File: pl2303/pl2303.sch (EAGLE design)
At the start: 3 parts, among them J1 ESP-STACK-HEADER, SW1 SW_TACT_2P-3X6

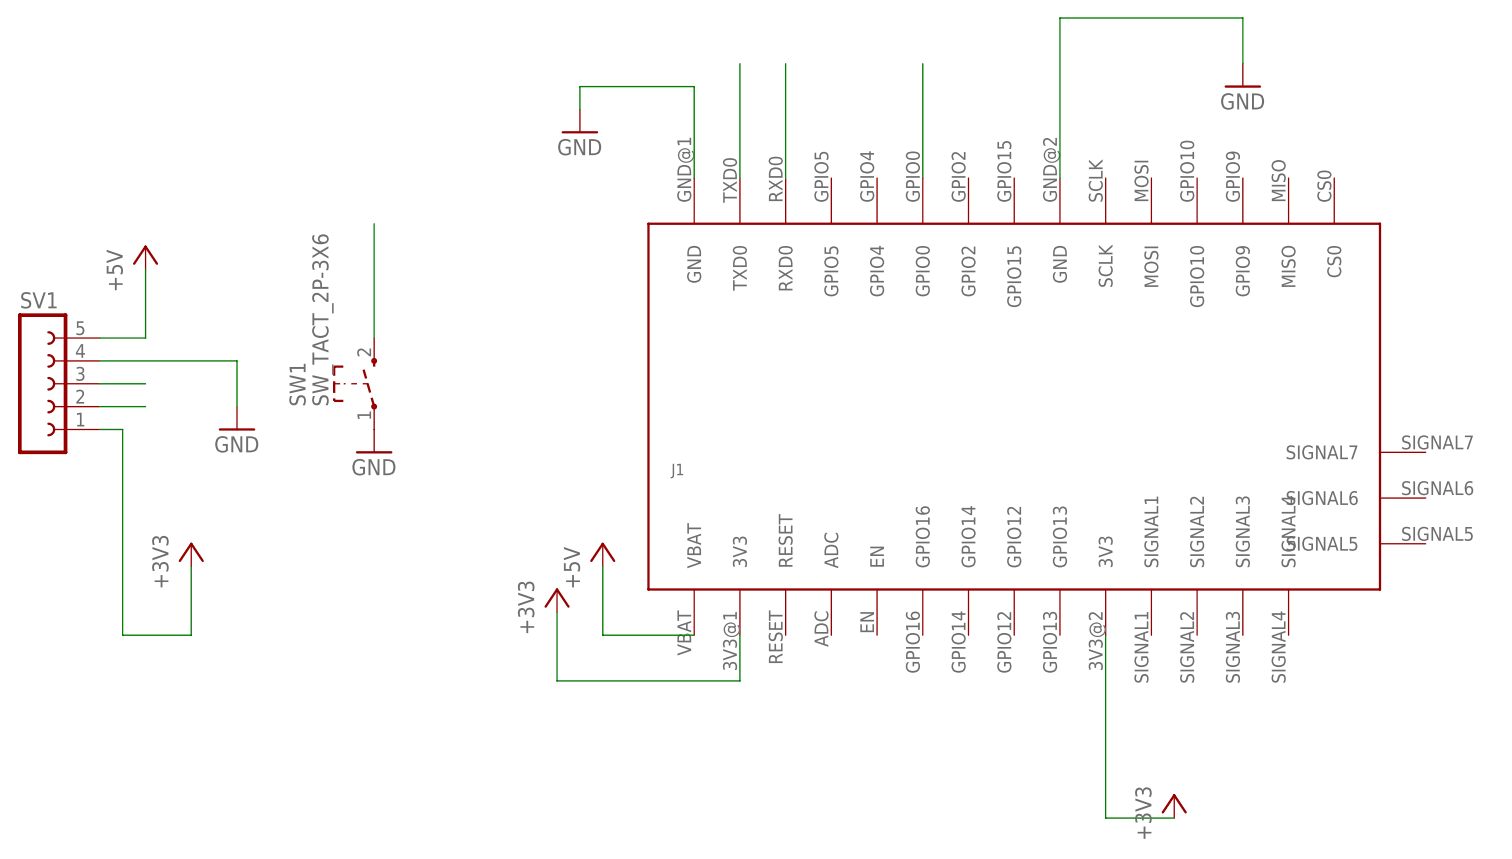
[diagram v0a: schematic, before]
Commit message: FTDI board update - new board size and mounting holes
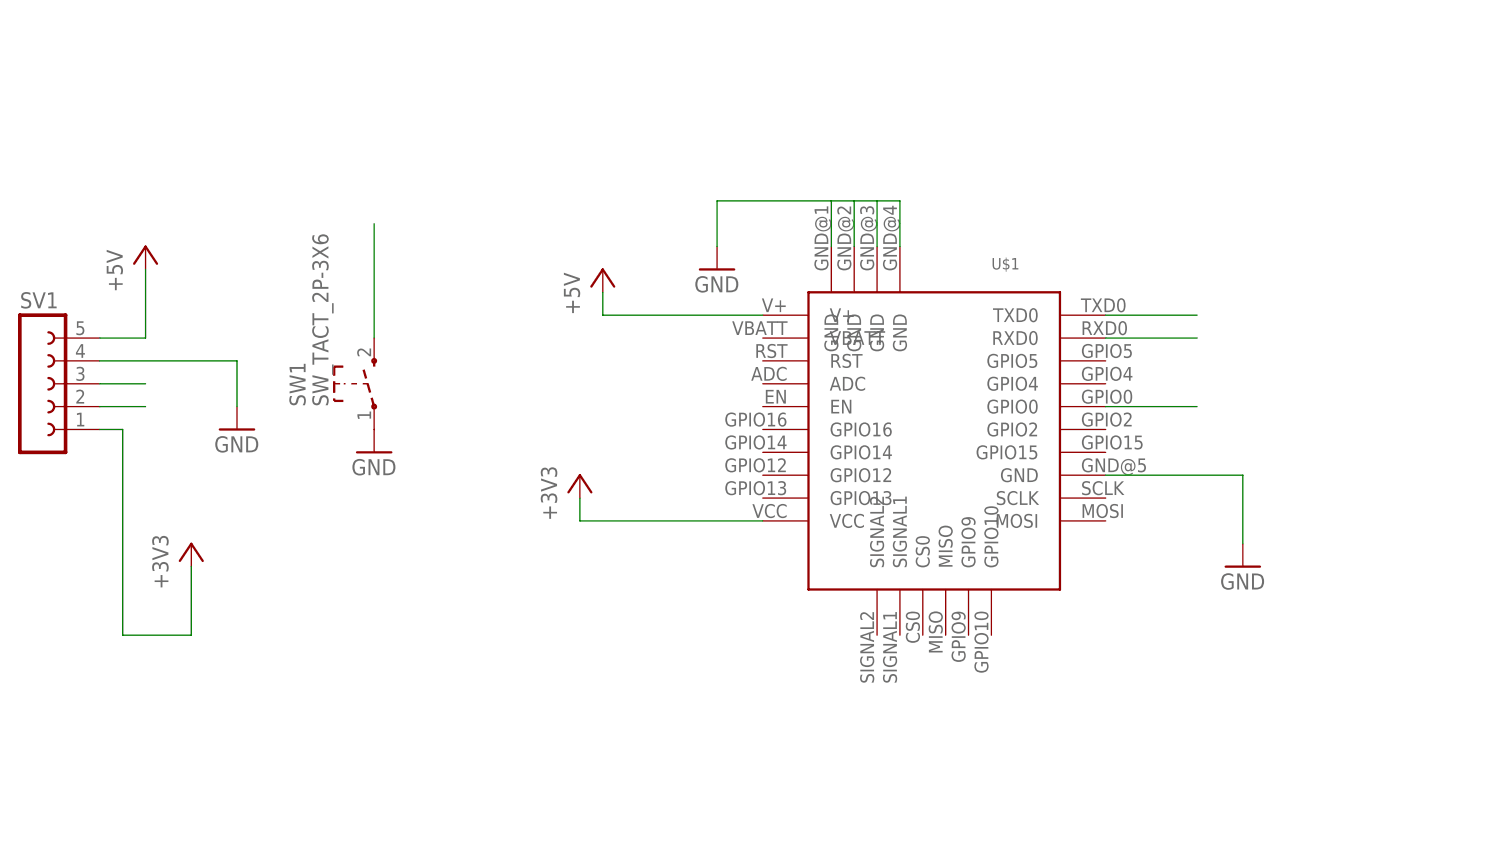
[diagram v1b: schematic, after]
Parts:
- removed J1: ESP-STACK-HEADER, ESPstack:ESP-STACK-HEADER
- added U$1: ESP-BOARD, ESPstack:ESP-BOARD
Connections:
- net +3V3: now also U$1.VCC; no longer J1.3V3@1, J1.3V3@2
- net +5V: now also U$1.V+; no longer J1.VBAT
- net GND: now also U$1.GND@1, U$1.GND@2, U$1.GND@3, U$1.GND@4, U$1.GND@5; no longer J1.GND@1, J1.GND@2
- net GPIO0: now also U$1.GPIO0; no longer J1.GPIO0
- net RXD0: now also U$1.RXD0; no longer J1.RXD0
- net TXD0: now also U$1.TXD0; no longer J1.TXD0
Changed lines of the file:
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@@
 <part name="P+1" library="supply1" deviceset="+5V" device=""/>
 <part name="+3V2" library="supply1" deviceset="+3V3" device=""/>
-<part name="J1" library="ESPstack" deviceset="ESP-STACK-HEADER" device=""/>
 <part name="+3V1" library="supply1" deviceset="+3V3" device=""/>
-<part name="+3V3" library="supply1" deviceset="+3V3" device=""/>
 <part name="P+2" library="supply1" deviceset="+5V" device=""/>
 <part name="GND1" library="supply1" deviceset="GND" device=""/>
@@
 <part name="SW1" library="dp_devices" deviceset="SW_TACT_2P" device="-3X6"/>
 <part name="GND4" library="supply1" deviceset="GND" device=""/>
+<part name="U$1" library="ESPstack" deviceset="ESP-BOARD" device=""/>
 </parts>
 <sheets>
@@
 <instance part="P+1" gate="1" x="7.62" y="71.12"/>
 <instance part="+3V2" gate="G$1" x="12.7" y="38.1"/>
-<instance part="J1" gate="G$1" x="83.82" y="53.34"/>
-<instance part="+3V1" gate="G$1" x="53.34" y="33.02"/>
-<instance part="+3V3" gate="G$1" x="121.92" y="10.16"/>
-<instance part="P+2" gate="1" x="58.42" y="38.1"/>
-<instance part="GND1" gate="1" x="129.54" y="88.9"/>
-<instance part="GND3" gate="1" x="55.88" y="83.82"/>
+<instance part="+3V1" gate="G$1" x="55.88" y="45.72"/>
+<instance part="P+2" gate="1" x="58.42" y="68.58"/>
+<instance part="GND1" gate="1" x="129.54" y="35.56"/>
+<instance part="GND3" gate="1" x="71.12" y="68.58"/>
 <instance part="SW1" gate="SW" x="33.02" y="55.88" rot="R90"/>
 <instance part="GND4" gate="1" x="33.02" y="48.26"/>
+<instance part="U$1" gate="G$1" x="93.98" y="50.8"/>
 </instances>
 <busses>
@@
 <net name="GND" class="0">
 <segment>
-<pinref part="J1" gate="G$1" pin="GND@2"/>
-<wire x1="109.22" y1="78.74" x2="109.22" y2="96.52" width="0.1524" layer="91"/>
-<wire x1="109.22" y1="96.52" x2="129.54" y2="96.52" width="0.1524" layer="91"/>
+<wire x1="129.54" y1="45.72" x2="129.54" y2="38.1" width="0.1524" layer="91"/>
 <pinref part="GND1" gate="1" pin="GND"/>
-<wire x1="129.54" y1="96.52" x2="129.54" y2="91.44" width="0.1524" layer="91"/>
+<pinref part="U$1" gate="G$1" pin="GND@5"/>
+<wire x1="129.54" y1="45.72" x2="114.3" y2="45.72" width="0.1524" layer="91"/>
 </segment>
 <segment>
-<pinref part="J1" gate="G$1" pin="GND@1"/>
-<wire x1="68.58" y1="78.74" x2="68.58" y2="88.9" width="0.1524" layer="91"/>
-<wire x1="68.58" y1="88.9" x2="55.88" y2="88.9" width="0.1524" layer="91"/>
-<wire x1="55.88" y1="88.9" x2="55.88" y2="86.36" width="0.1524" layer="91"/>
+<wire x1="91.44" y1="76.2" x2="88.9" y2="76.2" width="0.1524" layer="91"/>
+<wire x1="88.9" y1="76.2" x2="86.36" y2="76.2" width="0.1524" layer="91"/>
+<wire x1="86.36" y1="76.2" x2="83.82" y2="76.2" width="0.1524" layer="91"/>
+<wire x1="83.82" y1="76.2" x2="71.12" y2="76.2" width="0.1524" layer="91"/>
+<wire x1="71.12" y1="76.2" x2="71.12" y2="71.12" width="0.1524" layer="91"/>
 <pinref part="GND3" gate="1" pin="GND"/>
+<pinref part="U$1" gate="G$1" pin="GND@1"/>
+<wire x1="83.82" y1="71.12" x2="83.82" y2="76.2" width="0.1524" layer="91"/>
+<pinref part="U$1" gate="G$1" pin="GND@2"/>
+<wire x1="86.36" y1="71.12" x2="86.36" y2="76.2" width="0.1524" layer="91"/>
+<pinref part="U$1" gate="G$1" pin="GND@3"/>
+<wire x1="88.9" y1="71.12" x2="88.9" y2="76.2" width="0.1524" layer="91"/>
+<pinref part="U$1" gate="G$1" pin="GND@4"/>
+<wire x1="91.44" y1="76.2" x2="91.44" y2="71.12" width="0.1524" layer="91"/>
 </segment>
 <segment>
@@
 <net name="+5V" class="0">
 <segment>
-<pinref part="J1" gate="G$1" pin="VBAT"/>
-<wire x1="68.58" y1="27.94" x2="58.42" y2="27.94" width="0.1524" layer="91"/>
-<wire x1="58.42" y1="27.94" x2="58.42" y2="35.56" width="0.1524" layer="91"/>
+<wire x1="58.42" y1="63.5" x2="58.42" y2="66.04" width="0.1524" layer="91"/>
 <pinref part="P+2" gate="1" pin="+5V"/>
+<pinref part="U$1" gate="G$1" pin="V+"/>
+<wire x1="58.42" y1="63.5" x2="76.2" y2="63.5" width="0.1524" layer="91"/>
 </segment>
 <segment>
@@
 <net name="+3V3" class="0">
 <segment>
-<pinref part="J1" gate="G$1" pin="3V3@2"/>
-<pinref part="+3V3" gate="G$1" pin="+3V3"/>
-<wire x1="114.3" y1="27.94" x2="114.3" y2="7.62" width="0.1524" layer="91"/>
-<wire x1="114.3" y1="7.62" x2="121.92" y2="7.62" width="0.1524" layer="91"/>
-</segment>
-<segment>
-<pinref part="J1" gate="G$1" pin="3V3@1"/>
-<wire x1="73.66" y1="27.94" x2="73.66" y2="22.86" width="0.1524" layer="91"/>
 <pinref part="+3V1" gate="G$1" pin="+3V3"/>
-<wire x1="73.66" y1="22.86" x2="53.34" y2="22.86" width="0.1524" layer="91"/>
-<wire x1="53.34" y1="22.86" x2="53.34" y2="30.48" width="0.1524" layer="91"/>
+<wire x1="55.88" y1="40.64" x2="55.88" y2="43.18" width="0.1524" layer="91"/>
+<pinref part="U$1" gate="G$1" pin="VCC"/>
+<wire x1="55.88" y1="40.64" x2="76.2" y2="40.64" width="0.1524" layer="91"/>
 </segment>
 <segment>
@@
 <net name="TXD0" class="0">
 <segment>
-<pinref part="J1" gate="G$1" pin="TXD0"/>
-<wire x1="73.66" y1="78.74" x2="73.66" y2="91.44" width="0.1524" layer="91"/>
+<pinref part="SV1" gate="G$1" pin="3"/>
+<wire x1="2.54" y1="55.88" x2="7.62" y2="55.88" width="0.1524" layer="91"/>
 </segment>
 <segment>
-<pinref part="SV1" gate="G$1" pin="3"/>
-<wire x1="2.54" y1="55.88" x2="7.62" y2="55.88" width="0.1524" layer="91"/>
+<pinref part="U$1" gate="G$1" pin="TXD0"/>
+<wire x1="114.3" y1="63.5" x2="124.46" y2="63.5" width="0.1524" layer="91"/>
 </segment>
 </net>
 <net name="RXD0" class="0">
 <segment>
-<pinref part="J1" gate="G$1" pin="RXD0"/>
-<wire x1="78.74" y1="78.74" x2="78.74" y2="91.44" width="0.1524" layer="91"/>
+<pinref part="SV1" gate="G$1" pin="2"/>
+<wire x1="2.54" y1="53.34" x2="7.62" y2="53.34" width="0.1524" layer="91"/>
 </segment>
 <segment>
-<pinref part="SV1" gate="G$1" pin="2"/>
-<wire x1="2.54" y1="53.34" x2="7.62" y2="53.34" width="0.1524" layer="91"/>
+<pinref part="U$1" gate="G$1" pin="RXD0"/>
+<wire x1="114.3" y1="60.96" x2="124.46" y2="60.96" width="0.1524" layer="91"/>
 </segment>
 </net>
 <net name="GPIO0" class="0">
 <segment>
-<pinref part="J1" gate="G$1" pin="GPIO0"/>
-<wire x1="93.98" y1="78.74" x2="93.98" y2="91.44" width="0.1524" layer="91"/>
-</segment>
-<segment>
 <pinref part="SW1" gate="SW" pin="3"/>
 <wire x1="33.02" y1="60.96" x2="33.02" y2="73.66" width="0.1524" layer="91"/>
 </segment>
+<segment>
+<pinref part="U$1" gate="G$1" pin="GPIO0"/>
+<wire x1="114.3" y1="53.34" x2="124.46" y2="53.34" width="0.1524" layer="91"/>
+</segment>
 </net>

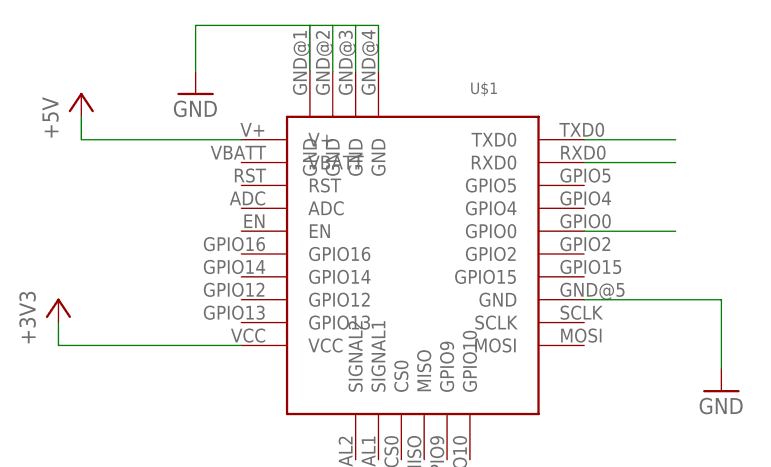
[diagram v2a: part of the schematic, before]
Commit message: New board schema applied to ftdi module
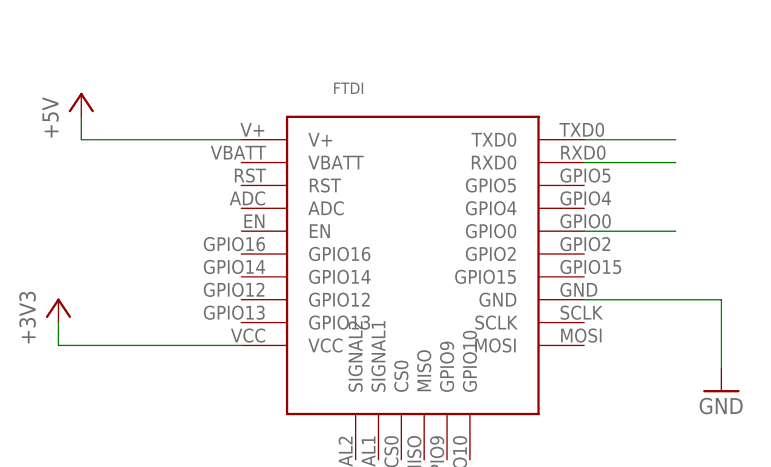
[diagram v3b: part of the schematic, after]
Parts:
- renumbered U$1 to FTDI
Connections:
- net GND: now also FTDI.GND; no longer FTDI.GND@1, FTDI.GND@2, FTDI.GND@3, FTDI.GND@4, FTDI.GND@5
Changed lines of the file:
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@@
 <part name="P+2" library="supply1" deviceset="+5V" device=""/>
 <part name="GND1" library="supply1" deviceset="GND" device=""/>
-<part name="GND3" library="supply1" deviceset="GND" device=""/>
 <part name="SW1" library="dp_devices" deviceset="SW_TACT_2P" device="-3X6"/>
 <part name="GND4" library="supply1" deviceset="GND" device=""/>
-<part name="U$1" library="ESPstack" deviceset="ESP-BOARD" device=""/>
+<part name="FTDI" library="ESPstack" deviceset="ESP-BOARD" device=""/>
 </parts>
 <sheets>
@@
 <instance part="P+2" gate="1" x="58.42" y="68.58"/>
 <instance part="GND1" gate="1" x="129.54" y="35.56"/>
-<instance part="GND3" gate="1" x="71.12" y="68.58"/>
 <instance part="SW1" gate="SW" x="33.02" y="55.88" rot="R90"/>
 <instance part="GND4" gate="1" x="33.02" y="48.26"/>
-<instance part="U$1" gate="G$1" x="93.98" y="50.8"/>
+<instance part="FTDI" gate="G$1" x="93.98" y="50.8"/>
 </instances>
 <busses>
@@
 <wire x1="129.54" y1="45.72" x2="129.54" y2="38.1" width="0.1524" layer="91"/>
 <pinref part="GND1" gate="1" pin="GND"/>
-<pinref part="U$1" gate="G$1" pin="GND@5"/>
+<pinref part="FTDI" gate="G$1" pin="GND"/>
 <wire x1="129.54" y1="45.72" x2="114.3" y2="45.72" width="0.1524" layer="91"/>
-</segment>
-<segment>
-<wire x1="91.44" y1="76.2" x2="88.9" y2="76.2" width="0.1524" layer="91"/>
-<wire x1="88.9" y1="76.2" x2="86.36" y2="76.2" width="0.1524" layer="91"/>
-<wire x1="86.36" y1="76.2" x2="83.82" y2="76.2" width="0.1524" layer="91"/>
-<wire x1="83.82" y1="76.2" x2="71.12" y2="76.2" width="0.1524" layer="91"/>
-<wire x1="71.12" y1="76.2" x2="71.12" y2="71.12" width="0.1524" layer="91"/>
-<pinref part="GND3" gate="1" pin="GND"/>
-<pinref part="U$1" gate="G$1" pin="GND@1"/>
-<wire x1="83.82" y1="71.12" x2="83.82" y2="76.2" width="0.1524" layer="91"/>
-<pinref part="U$1" gate="G$1" pin="GND@2"/>
-<wire x1="86.36" y1="71.12" x2="86.36" y2="76.2" width="0.1524" layer="91"/>
-<pinref part="U$1" gate="G$1" pin="GND@3"/>
-<wire x1="88.9" y1="71.12" x2="88.9" y2="76.2" width="0.1524" layer="91"/>
-<pinref part="U$1" gate="G$1" pin="GND@4"/>
-<wire x1="91.44" y1="76.2" x2="91.44" y2="71.12" width="0.1524" layer="91"/>
 </segment>
 <segment>
@@
 <wire x1="58.42" y1="63.5" x2="58.42" y2="66.04" width="0.1524" layer="91"/>
 <pinref part="P+2" gate="1" pin="+5V"/>
-<pinref part="U$1" gate="G$1" pin="V+"/>
+<pinref part="FTDI" gate="G$1" pin="V+"/>
 <wire x1="58.42" y1="63.5" x2="76.2" y2="63.5" width="0.1524" layer="91"/>
 </segment>
@@
 <pinref part="+3V1" gate="G$1" pin="+3V3"/>
 <wire x1="55.88" y1="40.64" x2="55.88" y2="43.18" width="0.1524" layer="91"/>
-<pinref part="U$1" gate="G$1" pin="VCC"/>
+<pinref part="FTDI" gate="G$1" pin="VCC"/>
 <wire x1="55.88" y1="40.64" x2="76.2" y2="40.64" width="0.1524" layer="91"/>
 </segment>
@@
 </segment>
 <segment>
-<pinref part="U$1" gate="G$1" pin="TXD0"/>
+<pinref part="FTDI" gate="G$1" pin="TXD0"/>
 <wire x1="114.3" y1="63.5" x2="124.46" y2="63.5" width="0.1524" layer="91"/>
 </segment>
@@
 </segment>
 <segment>
-<pinref part="U$1" gate="G$1" pin="RXD0"/>
+<pinref part="FTDI" gate="G$1" pin="RXD0"/>
 <wire x1="114.3" y1="60.96" x2="124.46" y2="60.96" width="0.1524" layer="91"/>
 </segment>
@@
 </segment>
 <segment>
-<pinref part="U$1" gate="G$1" pin="GPIO0"/>
+<pinref part="FTDI" gate="G$1" pin="GPIO0"/>
 <wire x1="114.3" y1="53.34" x2="124.46" y2="53.34" width="0.1524" layer="91"/>
 </segment>
